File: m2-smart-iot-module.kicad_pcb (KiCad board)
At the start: 4 copper layers, 80.2 x 22.1 mm, 167 parts, among them J1 MM8130-2600RA2, J2 2X05, J3 M.2-M+B-Pins, Q1 BSS123, SW1 PTS840_GK_SMTR_LFS, SW2 PTS840_GK_SMTR_LFS, U1 UPD720202, U10 MIC2877-5.0YFT-TR, U2 SST25VF512A, U3 CoralAccelerator, U4 NRF52840, U5 AP2120N-1.8TRG1, U6 AP22652W6-7, U7 TLV803EF29DBZR, U8 BME280, U9 NCP1599MNTWG, Y1 NX3225SA-24M, Y2 ABM11W-101-32.0000MHZ-T3, Y3 ABS06-32.768KHZ-9-1-T

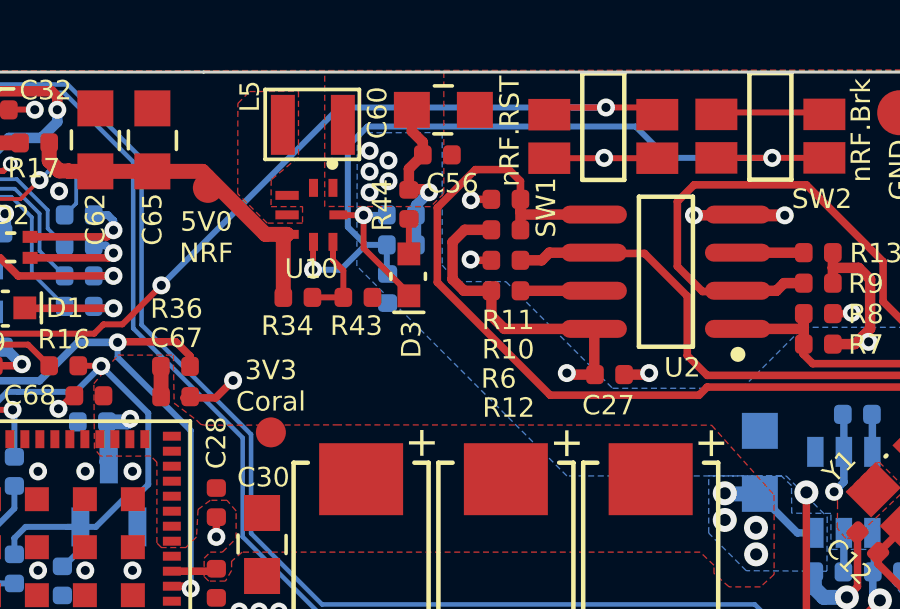
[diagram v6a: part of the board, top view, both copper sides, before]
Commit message: Adjust position of C56, add GND via near C56 and C60
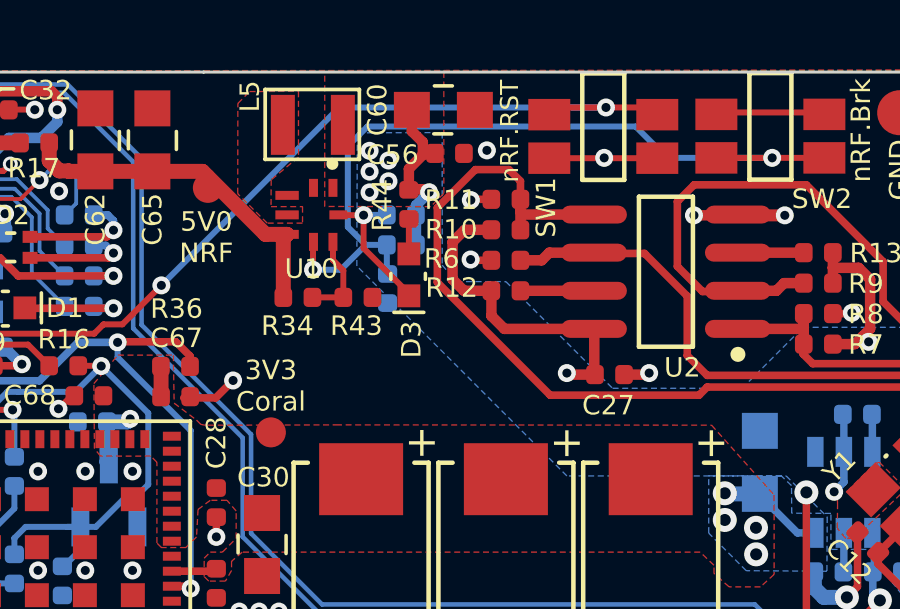
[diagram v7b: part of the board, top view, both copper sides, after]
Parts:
- moved C56 0.40 mm to (162.2, 94.2)
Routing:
- net GND: vias 185 -> 186
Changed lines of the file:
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@@
     (thickness 0.8)
     (drawings 138)
-    (tracks 1541)
+    (tracks 1542)
     (zones 0)
     (modules 167)
@@
     (0 F.Cu signal)
     (1 In1.Cu power)
-    (2 In2.Cu power hide)
+    (2 In2.Cu power)
     (31 B.Cu signal hide)
     (32 B.Adhes user hide)
@@
     (45 Margin user hide)
     (46 B.CrtYd user hide)
-    (47 F.CrtYd user hide)
+    (47 F.CrtYd user)
     (48 B.Fab user hide)
     (49 F.Fab user hide)
   )
   (setup
-    (last_trace_width 0.25)
+    (last_trace_width 0.128)
     (user_trace_width 0.128)
     (user_trace_width 0.182)
@@
     (at 162 92.7)
     (attr smd)
-    (fp_text reference C60 (at -2.2 0.1 90) (layer F.SilkS)
+    (fp_text reference C60 (at -2.2 0 90) (layer F.SilkS)
       (effects (font (size 0.65 0.65) (thickness 0.15)))
     )
@@
   )
   (module m2-smart-iot-module-footprints:0402-cap (layer F.Cu)
-    (at 161.8 94.2)
+    (at 162.2 94.15)
     (descr "Resistor SMD 0402 (1005 Metric), square (rectangular) end terminal, IPC_7351 nominal, (Body size source: http://www.tortai-tech.com/upload/download/2011102023233369053.pdf), generated with kicad-footprint-generator")
     (tags resistor)
     (attr smd)
-    (fp_text reference C56 (at 0.5 0.95) (layer F.SilkS)
+    (fp_text reference C56 (at -1.9 0.05) (layer F.SilkS)
       (effects (font (size 0.65 0.65) (thickness 0.15)))
     )
@@
     (tags resistor)
     (attr smd)
-    (fp_text reference R12 (at 0.092666 3.9002) (layer F.SilkS)
+    (fp_text reference R12 (at -1.807334 -0.0998) (layer F.SilkS)
       (effects (font (size 0.65 0.65) (thickness 0.15)))
     )
@@
     (tags resistor)
     (attr smd)
-    (fp_text reference R11 (at -0.076 -4.02828) (layer F.SilkS)
+    (fp_text reference R11 (at 1.834 -0.0182) (layer F.SilkS)
       (effects (font (size 0.65 0.65) (thickness 0.15)))
     )
@@
     (tags resistor)
     (attr smd)
-    (fp_text reference R10 (at 0.076 3.98732) (layer F.SilkS)
+    (fp_text reference R10 (at -1.824 -0.01268) (layer F.SilkS)
       (effects (font (size 0.65 0.65) (thickness 0.15)))
     )
@@
     (tags resistor)
     (attr smd)
-    (fp_text reference R6 (at 0.240667 -3.94636) (layer F.SilkS)
+    (fp_text reference R6 (at 2.140667 0.05364) (layer F.SilkS)
       (effects (font (size 0.65 0.65) (thickness 0.15)))
     )
@@
   )
   (gr_text nRF.RST (at 164.21 93.41 90) (layer F.SilkS)
-    (effects (font (size 0.65 0.65) (thickness 0.15)))
+    (effects (font (size 0.6 0.6) (thickness 0.15)))
   )
   (gr_line (start 115.021847 91.440116) (end 154.009145 91.440116) (layer Edge.Cuts) (width 0.1))
@@
   (segment (start 191.6 104.475) (end 191.025 104.475) (width 0.2) (layer F.Cu) (net 1))
   (segment (start 191.795395 107.347083) (end 190.947083 107.347083) (width 0.2) (layer F.Cu) (net 1))
+  (via (at 163.45 94.05) (size 0.6) (drill 0.3) (layers F.Cu B.Cu) (net 1))
   (via (at 159.54 94.065) (size 0.6) (drill 0.3) (layers F.Cu B.Cu) (net 2))
   (via (at 159.54 94.7575) (size 0.6) (drill 0.3) (layers F.Cu B.Cu) (net 2))

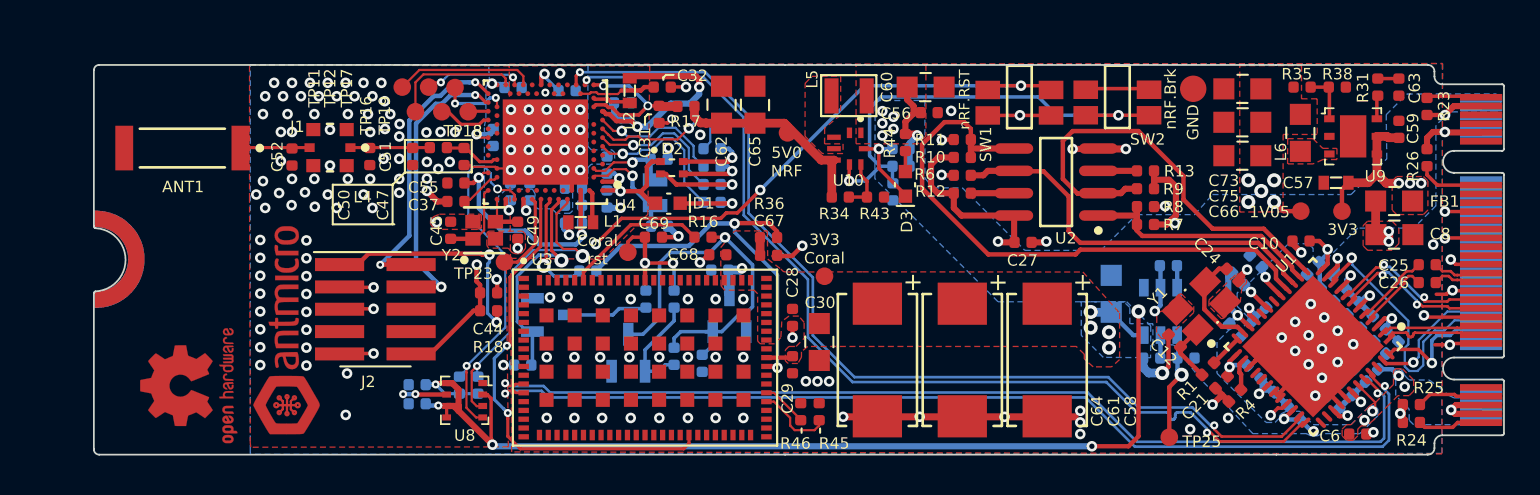
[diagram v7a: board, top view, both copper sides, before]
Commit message: Switched USB controller
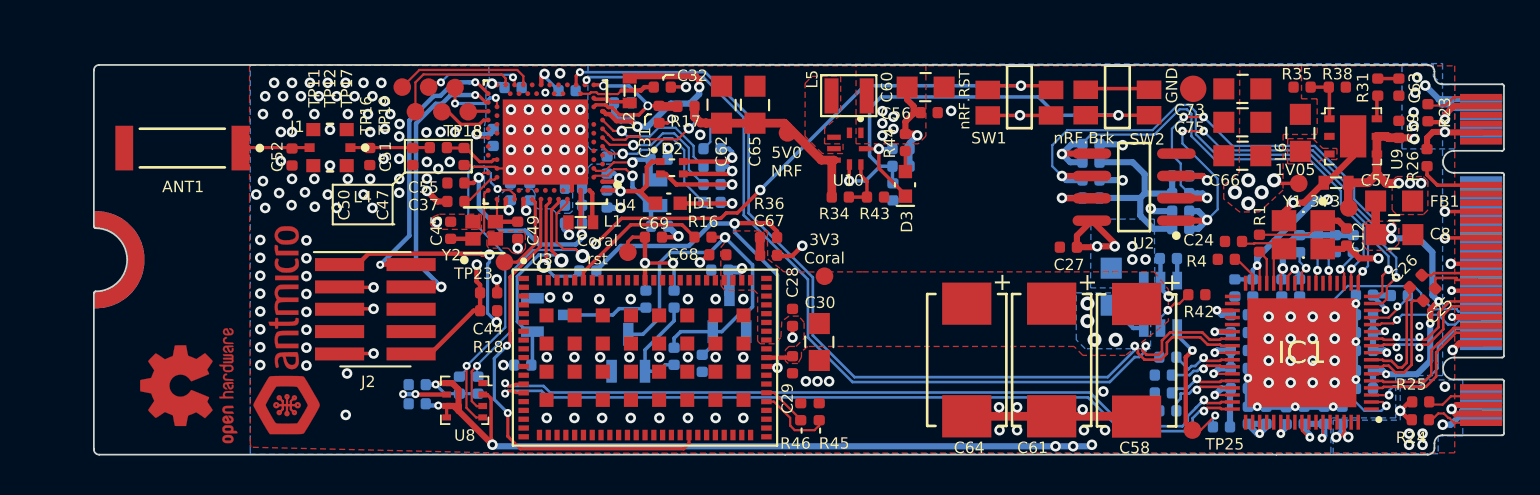
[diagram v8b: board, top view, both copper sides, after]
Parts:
- removed U1: UPD720202, m2-smart-iot-module-footprints:QFN48-Renesas-UPD720202
- added IC1: UPD720201K8-711-BAC-A, antmicro-footprints:QFN40P800X800X90-69N-D, F.Cu at (183.4, 107.8)
- added R47: ~, antmicro-footprints:0402-res, B.Cu at (185.3, 101.6)
- added R48: ~, antmicro-footprints:0402-res, B.Cu at (186.3, 101.6)
- added R49: R_0R_0402, antmicro-footprints:0402-res, B.Cu at (175.5, 109.1)
- added R50: R_0R_0402, antmicro-footprints:0402-res, B.Cu at (175.8, 108.1)
- added R51: R_0R_0402, antmicro-footprints:0402-res, B.Cu at (175.8, 111.1)
- added R52: R_0R_0402, antmicro-footprints:0402-res, B.Cu at (175.5, 110.1)
- C10, C21, C6, R10, R11, R12, R13, R6, R7, R8, R9: moved to B.Cu
- R42: moved to F.Cu
- moved C12 11.4 mm to (185.9, 101.2), turned to -90 degrees
- moved C6 8.86 mm to (179.8, 106.7)
- moved C11 8.59 mm to (180.3, 111.4), turned to 90 degrees
- moved C14 8.52 mm to (182.5, 111.4), turned to 90 degrees
- moved R4 7.76 mm to (179.1, 102.5), turned to 0 degrees
- moved R1 7.71 mm to (181.0, 101.6), turned to -90 degrees
- moved R10 7.32 mm to (171.4, 97.0), turned to 180 degrees
- moved R11 7.32 mm to (171.4, 96.0), turned to 0 degrees
- moved R12 7.32 mm to (171.4, 99.0), turned to 180 degrees
- moved R6 7.32 mm to (171.4, 98.0), turned to 0 degrees
- moved C22 7.30 mm to (179.8, 105.6), turned to 0 degrees
- moved Y1 7.08 mm to (183.5, 101.1), turned to 180 degrees
- moved C17 6.87 mm to (179.8, 108.7), turned to 0 degrees
- moved C9 6.68 mm to (183.5, 111.4), turned to 90 degrees
- moved C20 6.48 mm to (179.8, 107.7), turned to 0 degrees
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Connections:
- net /PCIe-USB-Bridge/XT2 renamed Net-(C24-Pad1)
- net /nRF52840/~RESET renamed /nRF52840/~{RESET}
- ANT1 pad 2: Net-(ANT1-Pad2) -> unconnected-(ANT1-Pad2)
- C25 pad 1: PERX_N -> /PCIe-USB-Bridge/PETXP
- C25 pad 2: /PCIe-USB-Bridge/PERXC_N -> PERX_P
- C26 pad 1: PERX_P -> /PCIe-USB-Bridge/PETXN
- C26 pad 2: /PCIe-USB-Bridge/PERXC_P -> PERX_N
- J2 pad 6: Net-(J2-Pad6) -> unconnected-(J2-Pad6)
- J2 pad 7: Net-(J2-Pad7) -> unconnected-(J2-Pad7)
- J2 pad 8: Net-(J2-Pad8) -> unconnected-(J2-Pad8)
- J3 pad 10: Net-(J3-Pad10) -> unconnected-(J3-Pad10)
- J3 pad 11: Net-(J3-Pad11) -> unconnected-(J3-Pad11)
- J3 pad 20: Net-(J3-Pad20) -> unconnected-(J3-Pad20)
- J3 pad 22: Net-(J3-Pad22) -> unconnected-(J3-Pad22)
- J3 pad 23: Net-(J3-Pad23) -> unconnected-(J3-Pad23)
- J3 pad 24: Net-(J3-Pad24) -> unconnected-(J3-Pad24)
- J3 pad 25: Net-(J3-Pad25) -> unconnected-(J3-Pad25)
- J3 pad 26: Net-(J3-Pad26) -> unconnected-(J3-Pad26)
- J3 pad 28: Net-(J3-Pad28) -> unconnected-(J3-Pad28)
- J3 pad 29: Net-(J3-Pad29) -> unconnected-(J3-Pad29)
- J3 pad 30: Net-(J3-Pad30) -> unconnected-(J3-Pad30)
- J3 pad 31: Net-(J3-Pad31) -> unconnected-(J3-Pad31)
- J3 pad 32: Net-(J3-Pad32) -> unconnected-(J3-Pad32)
- J3 pad 34: Net-(J3-Pad34) -> unconnected-(J3-Pad34)
- J3 pad 35: Net-(J3-Pad35) -> unconnected-(J3-Pad35)
- J3 pad 36: Net-(J3-Pad36) -> unconnected-(J3-Pad36)
- J3 pad 37: Net-(J3-Pad37) -> unconnected-(J3-Pad37)
- J3 pad 38: Net-(J3-Pad38) -> unconnected-(J3-Pad38)
- J3 pad 40: Net-(J3-Pad40) -> unconnected-(J3-Pad40)
- J3 pad 42: Net-(J3-Pad42) -> unconnected-(J3-Pad42)
- J3 pad 44: Net-(J3-Pad44) -> unconnected-(J3-Pad44)
- J3 pad 46: Net-(J3-Pad46) -> unconnected-(J3-Pad46)
- J3 pad 48: Net-(J3-Pad48) -> unconnected-(J3-Pad48)
- J3 pad 5: Net-(J3-Pad5) -> unconnected-(J3-Pad5)
- J3 pad 50: ~PERST -> ~{PERST}
- J3 pad 52: ~PECREQ -> ~{PECREQ}
- J3 pad 54: ~PEWAKE -> ~{PEWAKE}
- J3 pad 56: Net-(J3-Pad56) -> unconnected-(J3-Pad56)
- J3 pad 58: Net-(J3-Pad58) -> unconnected-(J3-Pad58)
- J3 pad 6: Net-(J3-Pad6) -> unconnected-(J3-Pad6)
- J3 pad 67: Net-(J3-Pad67) -> unconnected-(J3-Pad67)
- J3 pad 68: Net-(J3-Pad68) -> unconnected-(J3-Pad68)
- J3 pad 7: Net-(J3-Pad7) -> unconnected-(J3-Pad7)
- J3 pad 8: Net-(J3-Pad8) -> unconnected-(J3-Pad8)
- R1 pad 2: /PCIe-USB-Bridge/XT1 -> Net-(R1-Pad2)
- R4 pad 1: Net-(R4-Pad1) -> GND
- R4 pad 2: GND -> Net-(R4-Pad2)
- U3 pad 4: Net-(U3-Pad4) -> unconnected-(U3-Pad4)
- U3 pad 5: Net-(U3-Pad5) -> unconnected-(U3-Pad5)
- U3 pad 52: Net-(U3-Pad52) -> unconnected-(U3-Pad52)
- U3 pad 77: Net-(U3-Pad77) -> unconnected-(U3-Pad77)
- U3 pad 78: Net-(U3-Pad78) -> unconnected-(U3-Pad78)
- U3 pad 82: Net-(U3-Pad82) -> unconnected-(U3-Pad82)
- U3 pad 84: Net-(U3-Pad84) -> unconnected-(U3-Pad84)
- U3 pad 85: Net-(U3-Pad85) -> unconnected-(U3-Pad85)
- U4 pad AC11: Net-(U4-PadAC11) -> unconnected-(U4-PadAC11)
- U4 pad AC15: Net-(U4-PadAC15) -> unconnected-(U4-PadAC15)
- U4 pad AC17: Net-(U4-PadAC17) -> unconnected-(U4-PadAC17)
- U4 pad AC19: Net-(U4-PadAC19) -> unconnected-(U4-PadAC19)
- U4 pad AC21: Net-(U4-PadAC21) -> unconnected-(U4-PadAC21)
- U4 pad AC9: Net-(U4-PadAC9) -> unconnected-(U4-PadAC9)
- U4 pad AD10: Net-(U4-PadAD10) -> unconnected-(U4-PadAD10)
- U4 pad AD12: Net-(U4-PadAD12) -> unconnected-(U4-PadAD12)
- U4 pad AD16: Net-(U4-PadAD16) -> unconnected-(U4-PadAD16)
- U4 pad AD8: Net-(U4-PadAD8) -> unconnected-(U4-PadAD8)
- U4 pad B11: Net-(U4-PadB11) -> unconnected-(U4-PadB11)
- U4 pad B13: Net-(U4-PadB13) -> unconnected-(U4-PadB13)
- U4 pad B15: Net-(U4-PadB15) -> unconnected-(U4-PadB15)
- U4 pad B17: Net-(U4-PadB17) -> unconnected-(U4-PadB17)
- U4 pad B19: Net-(U4-PadB19) -> unconnected-(U4-PadB19)
- U4 pad B9: Net-(U4-PadB9) -> unconnected-(U4-PadB9)
- U4 pad G1: Net-(U4-PadG1) -> unconnected-(U4-PadG1)
- U4 pad H2: Net-(U4-PadH2) -> unconnected-(U4-PadH2)
- U4 pad J1: Net-(U4-PadJ1) -> unconnected-(U4-PadJ1)
- U4 pad J24: Net-(U4-PadJ24) -> unconnected-(U4-PadJ24)
- U4 pad K2: Net-(U4-PadK2) -> unconnected-(U4-PadK2)
- U4 pad L24: Net-(U4-PadL24) -> unconnected-(U4-PadL24)
- U4 pad M2: Net-(U4-PadM2) -> unconnected-(U4-PadM2)
- U4 pad P2: Net-(U4-PadP2) -> unconnected-(U4-PadP2)
- U4 pad P23: Net-(U4-PadP23) -> unconnected-(U4-PadP23)
- U4 pad R24: Net-(U4-PadR24) -> unconnected-(U4-PadR24)
- U4 pad T2: Net-(U4-PadT2) -> unconnected-(U4-PadT2)
- U4 pad T23: Net-(U4-PadT23) -> unconnected-(U4-PadT23)
- U4 pad V23: Net-(U4-PadV23) -> unconnected-(U4-PadV23)
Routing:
- net 1V05: track 81.5 -> 23.5 mm, vias 12 -> 14
- net ~{PERST}: track 0.00 -> 19.8 mm, vias 0 -> 1
- net /PCIe-USB-Bridge/SPICSB: track 13.9 -> 29.9 mm, vias 0 -> 4
- net ~PECREQ: track 15.9 -> 0.00 mm, vias 1 -> 0
- net CORAL_USB_N: track 57.3 -> 44.2 mm
- net CORAL_USB_P: track 56.6 -> 44.4 mm
- net /PCIe-USB-Bridge/SPISCK: track 22.4 -> 31.4 mm, vias 0 -> 2
- net ~{PEWAKE}: track 0.00 -> 8.64 mm, vias 0 -> 1
- net ~PERST: track 7.58 -> 0.00 mm, vias 1 -> 0
- net ~PEWAKE: track 7.20 -> 0.00 mm, vias 1 -> 0
- net /PCIe-USB-Bridge/PETXP: track 0.00 -> 6.89 mm
- net ~{PECREQ}: track 0.00 -> 6.80 mm, vias 0 -> 1
- net /PCIe-USB-Bridge/PETXN: track 0.00 -> 6.66 mm
- net /PCIe-USB-Bridge/AVDD: track 25.3 -> 31.1 mm, vias 4 -> 7
- net /PCIe-USB-Bridge/SPISI: track 34.0 -> 28.7 mm, vias 0 -> 2
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- added copper zone on In2.Cu, net 1V05
- added copper zone on In2.Cu, net 3V3
- removed copper zone on In1.Cu, net 1V05
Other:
- net class Default removed
- net class Diff_100 removed
- net class Diff_90 removed
